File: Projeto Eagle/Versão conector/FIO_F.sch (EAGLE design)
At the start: 4 parts, among them J1 CONECTOR_FEMEA

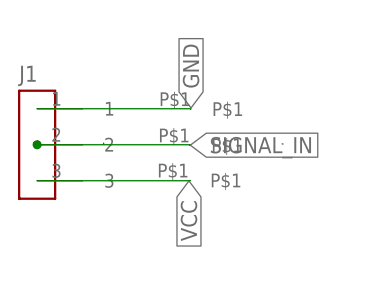
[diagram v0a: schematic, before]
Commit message: correção de pads e adição de label de versionamento
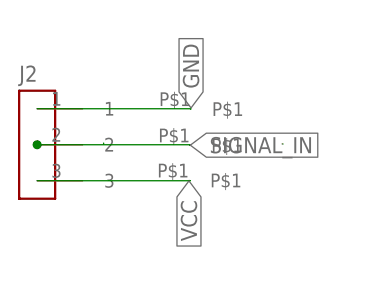
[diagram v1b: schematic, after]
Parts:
- renumbered J1 to J2, U$2 to J4
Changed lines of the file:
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@@
 </classes>
 <parts>
-<part name="J1" library="Eletroblocks Lib" deviceset="CONECTOR_FEMEA" device="" override_package3d_urn="urn:adsk.eagle:package:22394112/2" override_package_urn="urn:adsk.eagle:footprint:22394113/1"/>
+<part name="J2" library="Eletroblocks Lib" deviceset="CONECTOR_FEMEA" device="" override_package3d_urn="urn:adsk.eagle:package:22394112/2" override_package_urn="urn:adsk.eagle:footprint:22394113/1" override_locally_modified="yes"/>
 <part name="U$1" library="Eletroblocks Lib" deviceset="PAD" device=""/>
-<part name="U$2" library="Eletroblocks Lib" deviceset="PAD" device="" override_package3d_urn="urn:adsk.eagle:package:22394060/2" override_package_urn="urn:adsk.eagle:footprint:22394061/1"/>
+<part name="J4" library="Eletroblocks Lib" deviceset="PAD" device="" override_package3d_urn="urn:adsk.eagle:package:22394060/4" override_package_urn="urn:adsk.eagle:footprint:22394061/2"/>
 <part name="VCC" library="Eletroblocks Lib" deviceset="PAD" device=""/>
 </parts>
@@
 </plain>
 <instances>
-<instance part="J1" gate="G$1" x="4.52" y="100.65" smashed="yes">
+<instance part="J2" gate="G$1" x="4.52" y="100.65" smashed="yes">
 <attribute name="NAME" x="2.52" y="107.65" size="1.778" layer="95"/>
 </instance>
 <instance part="U$1" gate="G$1" x="21.59" y="104.61" smashed="yes"/>
-<instance part="U$2" gate="G$1" x="21.51" y="100.58" smashed="yes"/>
+<instance part="J4" gate="G$1" x="21.51" y="100.58" smashed="yes"/>
 <instance part="VCC" gate="G$1" x="21.39" y="96.68" smashed="yes"/>
 </instances>
@@
 </segment>
 <segment>
-<pinref part="J1" gate="G$1" pin="2"/>
+<pinref part="J2" gate="G$1" pin="2"/>
 <wire x1="4.52" y1="100.65" x2="4.52" y2="100.61" width="0.1524" layer="91"/>
-<pinref part="U$2" gate="G$1" pin="P$1"/>
+<pinref part="J4" gate="G$1" pin="P$1"/>
 <wire x1="4.52" y1="100.65" x2="21.57" y2="100.65" width="0.1524" layer="91"/>
 <wire x1="21.57" y1="100.65" x2="21.51" y2="100.58" width="0.1524" layer="91"/>
@@
 <net name="GND" class="0">
 <segment>
-<pinref part="J1" gate="G$1" pin="1"/>
+<pinref part="J2" gate="G$1" pin="1"/>
 <pinref part="U$1" gate="G$1" pin="P$1"/>
 <wire x1="4.52" y1="104.65" x2="21.59" y2="104.65" width="0.1524" layer="91"/>
@@
 <net name="VCC" class="0">
 <segment>
-<pinref part="J1" gate="G$1" pin="3"/>
+<pinref part="J2" gate="G$1" pin="3"/>
 <pinref part="VCC" gate="G$1" pin="P$1"/>
 <wire x1="4.52" y1="96.65" x2="21.51" y2="96.65" width="0.1524" layer="91"/>
